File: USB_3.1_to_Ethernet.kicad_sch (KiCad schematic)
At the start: 62 parts, among them J1 RJ45_JK0654219, U1 LAN7801_9JX, U2 93LC56B_SN, U3 KSZ9031RNXCC, Y1 25MHz, Y2 25MHz

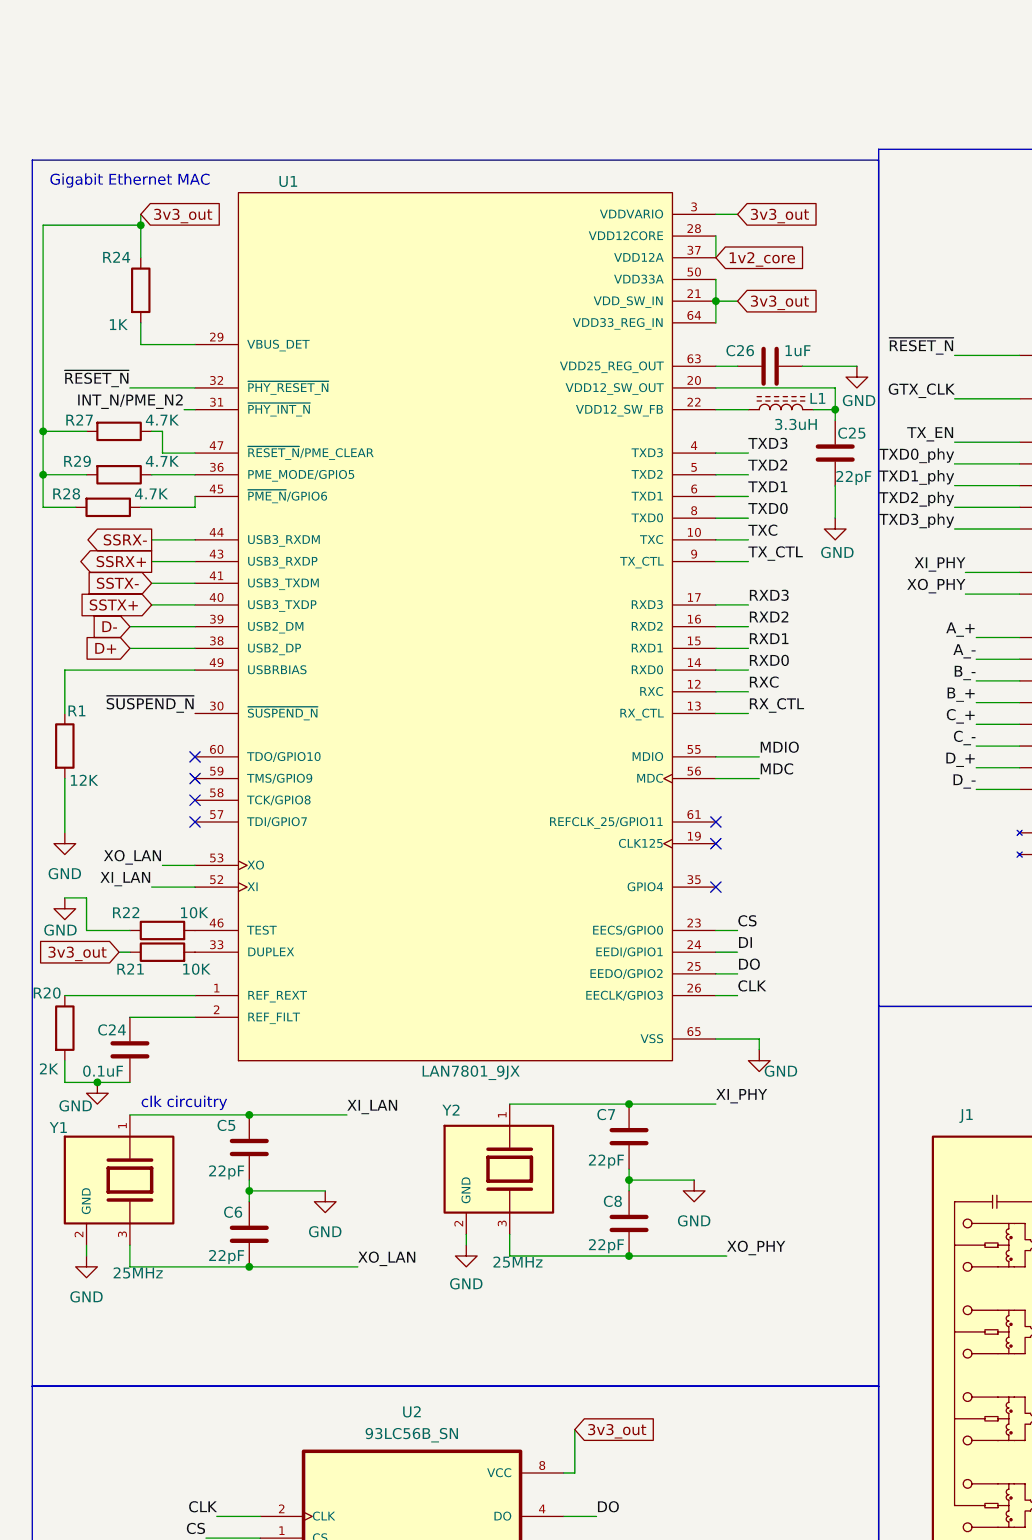
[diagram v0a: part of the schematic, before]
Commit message: some minor changes in the routing
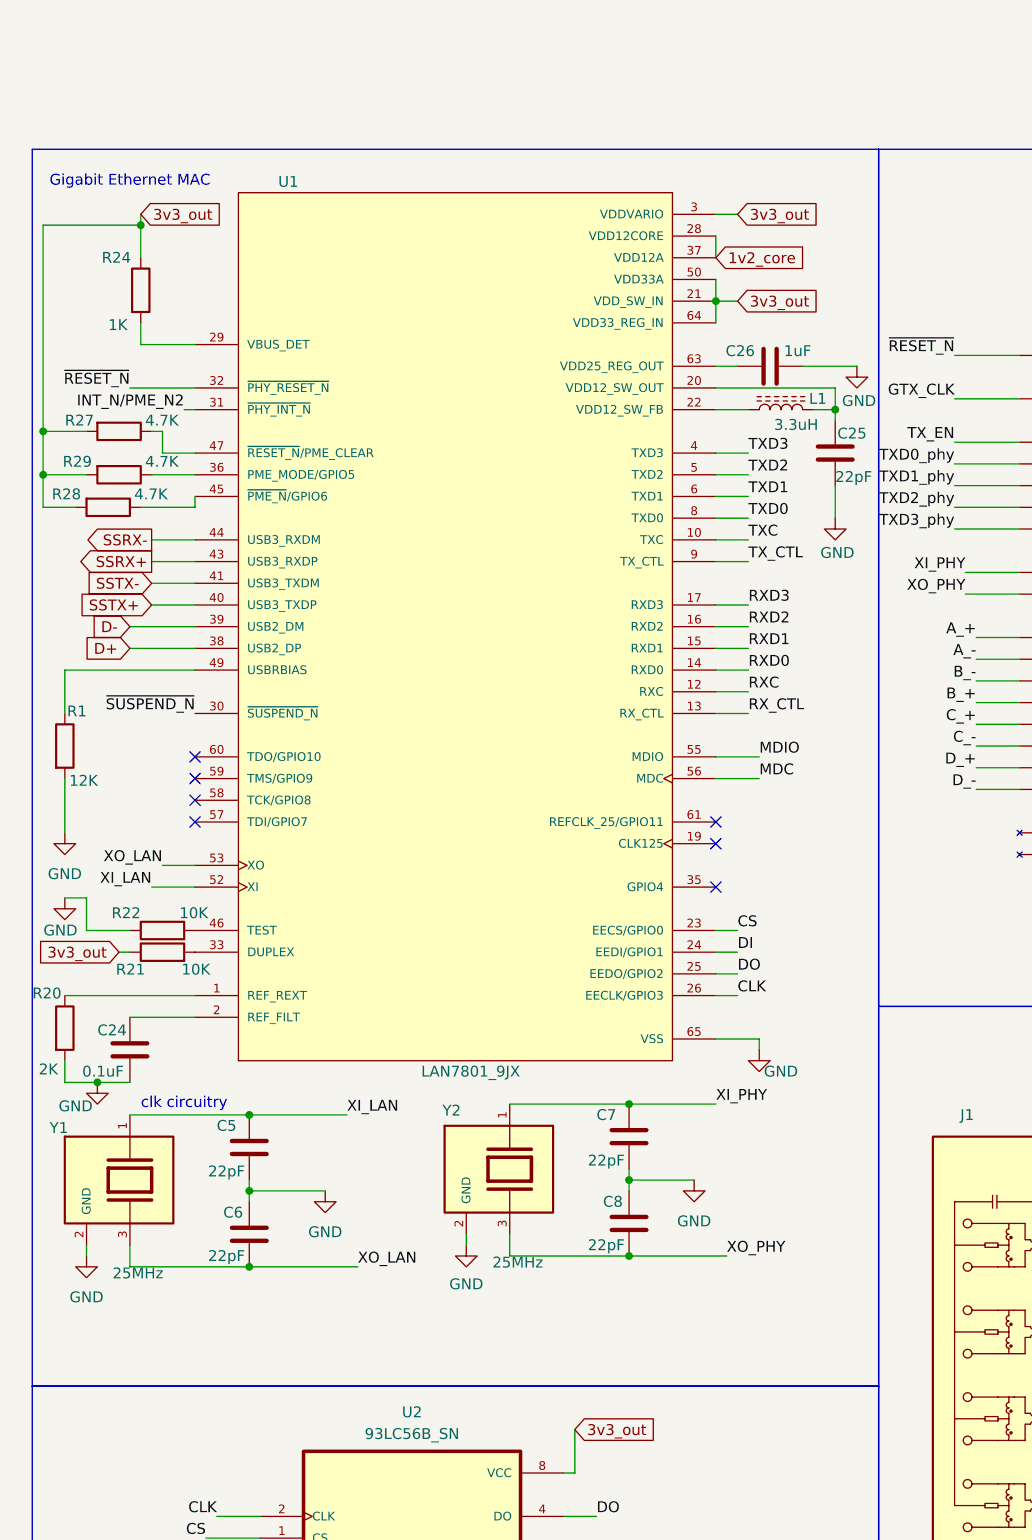
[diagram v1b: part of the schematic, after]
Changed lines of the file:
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@@
 	)
 	(rectangle
-		(start 12.7 13.97)
+		(start 12.7 12.7)
 		(end 111.76 157.48)
 		(stroke

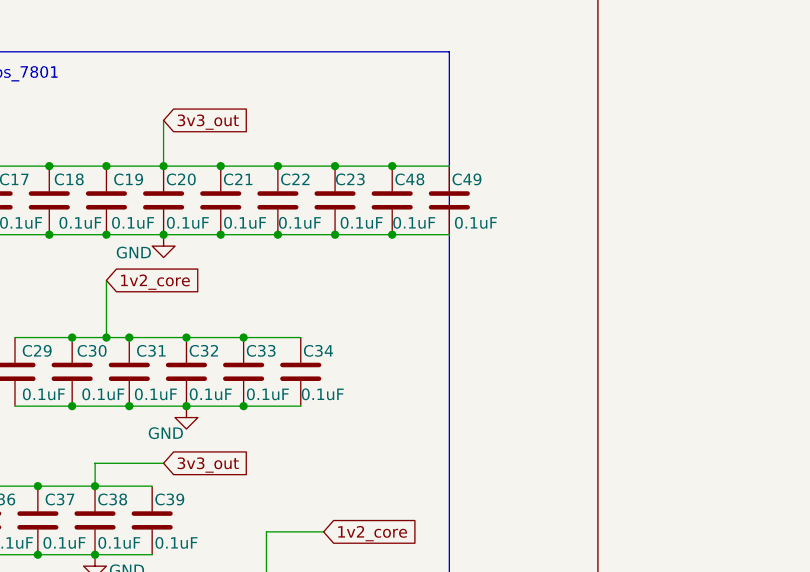
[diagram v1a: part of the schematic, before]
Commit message: resolved drc errors of shorting nets
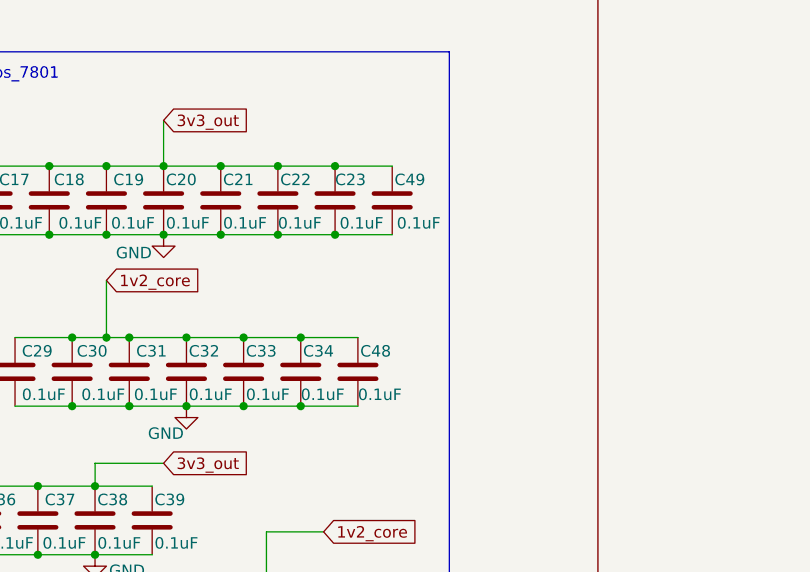
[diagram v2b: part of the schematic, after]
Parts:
- U3: footprint KSZ9031RNX:IC_KSZ9031RNXCC -> KSZ9031RNXCC:IC_KSZ9031RNXCC
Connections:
- net AVDDH: no longer C48.1
- net AVDDL: now also C48.1
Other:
- moved on the sheet: C48, C49
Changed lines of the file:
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@@
 	)
 	(junction
-		(at 278.13 25.4)
-		(diameter 0)
-		(color 0 0 0 0)
-	)
-	(junction
-		(at 271.78 33.02)
-		(diameter 0)
-		(color 0 0 0 0)
-	)
-	(junction
 		(at 252.73 33.02)
 		(diameter 0)
@@
 	)
 	(junction
-		(at 238.76 80.01)
+		(at 271.78 33.02)
 		(diameter 0)
 		(color 0 0 0 0)
 	)
 	(junction
-		(at 261.62 52.07)
+		(at 267.97 52.07)
 		(diameter 0)
 		(color 0 0 0 0)
 	)
 	(junction
-		(at 271.78 25.4)
+		(at 238.76 80.01)
+		(diameter 0)
+		(color 0 0 0 0)
+	)
+	(junction
+		(at 261.62 52.07)
 		(diameter 0)
 		(color 0 0 0 0)
@@
 	)
 	(junction
-		(at 259.08 33.02)
+		(at 271.78 25.4)
 		(diameter 0)
 		(color 0 0 0 0)
 	)
 	(junction
-		(at 242.57 44.45)
+		(at 259.08 33.02)
 		(diameter 0)
 		(color 0 0 0 0)
 	)
 	(junction
-		(at 278.13 33.02)
+		(at 242.57 44.45)
 		(diameter 0)
 		(color 0 0 0 0)
@@
 	)
 	(junction
+		(at 267.97 44.45)
+		(diameter 0)
+		(color 0 0 0 0)
+	)
+	(junction
 		(at 255.27 52.07)
 		(diameter 0)
@@
 	(wire
 		(pts
-			(xy 271.78 33.02) (xy 278.13 33.02)
-		)
-		(stroke
-			(width 0)
-			(type default)
-		)
-	)
-	(wire
-		(pts
 			(xy 24.13 71.12) (xy 31.75 71.12)
 		)
@@
 	(wire
 		(pts
-			(xy 271.78 25.4) (xy 278.13 25.4)
-		)
-		(stroke
-			(width 0)
-			(type default)
-		)
-	)
-	(wire
-		(pts
 			(xy 26.67 45.72) (xy 27.94 45.72)
 		)
@@
 	(wire
 		(pts
-			(xy 278.13 25.4) (xy 284.48 25.4)
+			(xy 271.78 25.4) (xy 278.13 25.4)
 		)
 		(stroke
@@
 	(wire
 		(pts
+			(xy 267.97 44.45) (xy 274.32 44.45)
+		)
+		(stroke
+			(width 0)
+			(type default)
+		)
+	)
+	(wire
+		(pts
 			(xy 121.92 62.23) (xy 128.27 62.23)
 		)
@@
 	(wire
 		(pts
-			(xy 278.13 33.02) (xy 284.48 33.02)
+			(xy 271.78 33.02) (xy 278.13 33.02)
 		)
 		(stroke
@@
 	(wire
 		(pts
+			(xy 267.97 52.07) (xy 274.32 52.07)
+		)
+		(stroke
+			(width 0)
+			(type default)
+		)
+	)
+	(wire
+		(pts
 			(xy 96.52 78.74) (xy 92.71 78.74)
 		)
@@
 	(symbol
 		(lib_id "Device:C")
-		(at 278.13 29.21 0)
+		(at 274.32 48.26 0)
 		(unit 1)
 		(body_style 1)
@@
 		(dnp no)
 		(property "Reference" "C48"
-			(at 278.384 26.924 0)
+			(at 274.574 45.974 0)
 			(show_name no)
 			(do_not_autoplace no)
@@
 		)
 		(property "Value" "0.1uF"
-			(at 278.13 31.75 0)
+			(at 274.32 50.8 0)
 			(show_name no)
 			(do_not_autoplace no)
@@
 		)
 		(property "Footprint" "Capacitor_SMD:C_01005_0402Metric"
-			(at 279.0952 33.02 0)
+			(at 275.2852 52.07 0)
 			(hide yes)
 			(show_name no)
@@
 		)
 		(property "Datasheet" ""
-			(at 278.13 29.21 0)
+			(at 274.32 48.26 0)
 			(hide yes)
 			(show_name no)
@@
 		)
 		(property "Description" "Unpolarized capacitor"
-			(at 278.13 29.21 0)
+			(at 274.32 48.26 0)
 			(hide yes)
 			(show_name no)
@@
 			)
 		)
-		(property "Footprint" "KSZ9031RNX:IC_KSZ9031RNXCC"
+		(property "Footprint" "KSZ9031RNXCC:IC_KSZ9031RNXCC"
 			(at 153.67 59.69 0)
 			(hide yes)
@@
 	(symbol
 		(lib_id "Device:C")
-		(at 284.48 29.21 0)
+		(at 278.13 29.21 0)
 		(unit 1)
 		(body_style 1)
@@
 		(dnp no)
 		(property "Reference" "C49"
-			(at 284.734 26.924 0)
+			(at 278.384 26.924 0)
 			(show_name no)
 			(do_not_autoplace no)
@@
 		)
 		(property "Value" "0.1uF"
-			(at 284.988 31.75 0)
+			(at 278.638 31.75 0)
 			(show_name no)
 			(do_not_autoplace no)
@@
 		)
 		(property "Footprint" "Capacitor_SMD:C_01005_0402Metric"
-			(at 285.4452 33.02 0)
+			(at 279.0952 33.02 0)
 			(hide yes)
 			(show_name no)
@@
 		)
 		(property "Datasheet" ""
-			(at 284.48 29.21 0)
+			(at 278.13 29.21 0)
 			(hide yes)
 			(show_name no)
@@
 		)
 		(property "Description" "Unpolarized capacitor"
-			(at 284.48 29.21 0)
+			(at 278.13 29.21 0)
 			(hide yes)
 			(show_name no)
